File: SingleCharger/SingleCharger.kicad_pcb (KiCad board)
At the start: 2 copper layers, 120 x 130 mm, 59 parts, among them J1 Bus_PCI_Express_x1, Q2 TPHR8504PL,LQ(M1W, U1 ADS1115IDGSR, U10 LM358, U11 MCP4725A0T-E/CH, U2 PICO, U3 TPS54360BDDAR, U4 TPS54360BDDAR, U8 UCC27324DR, U9 LM393

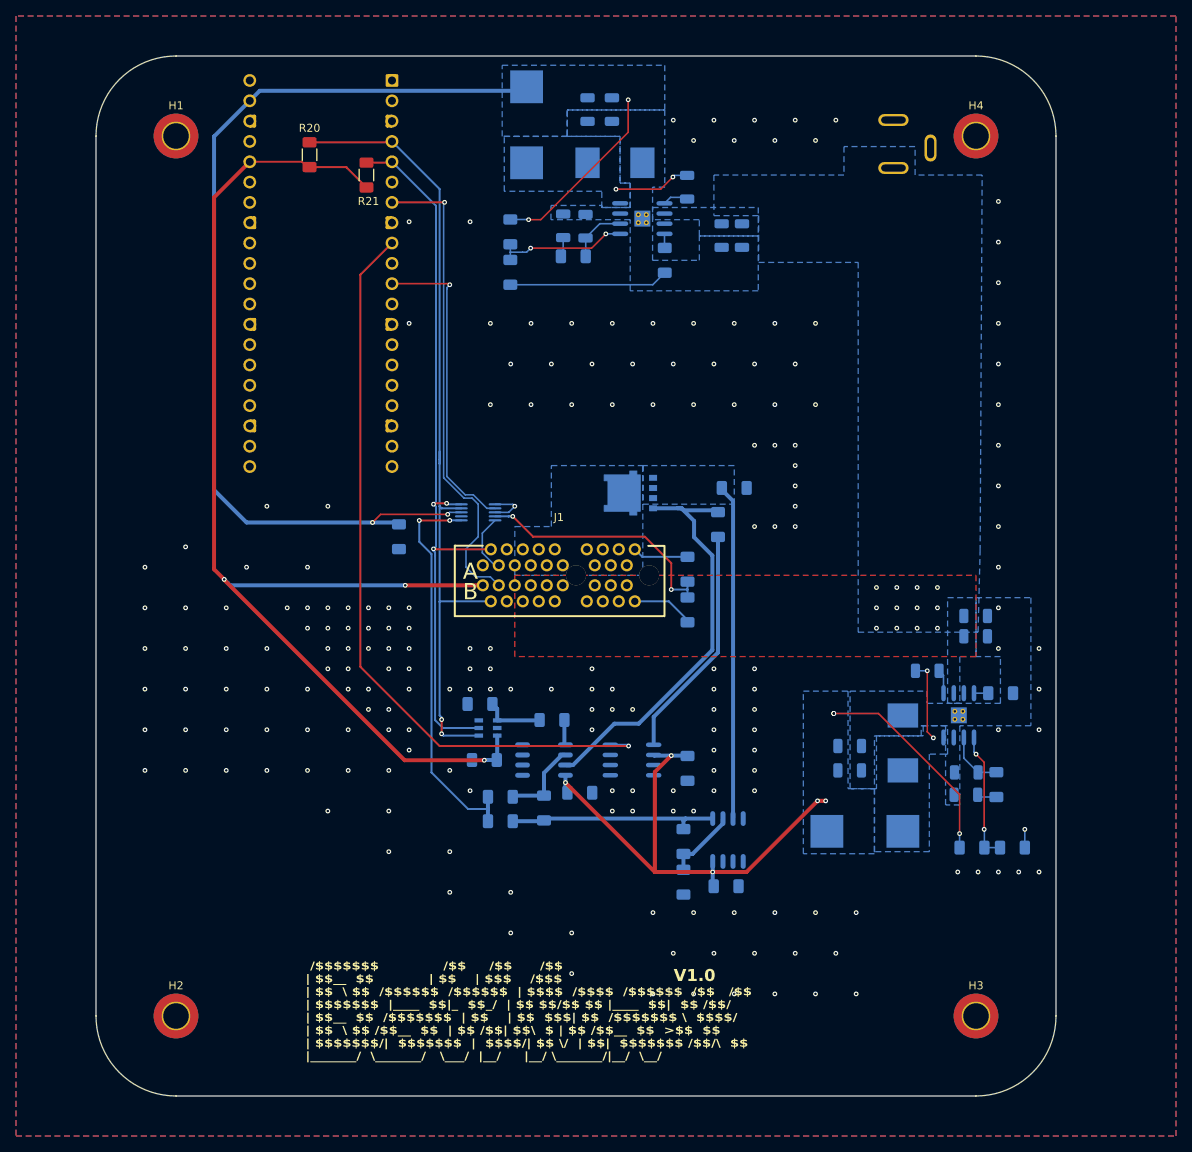
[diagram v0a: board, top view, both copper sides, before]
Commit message: Moved to +48V Feed. 25.2 Controlled by Pico.
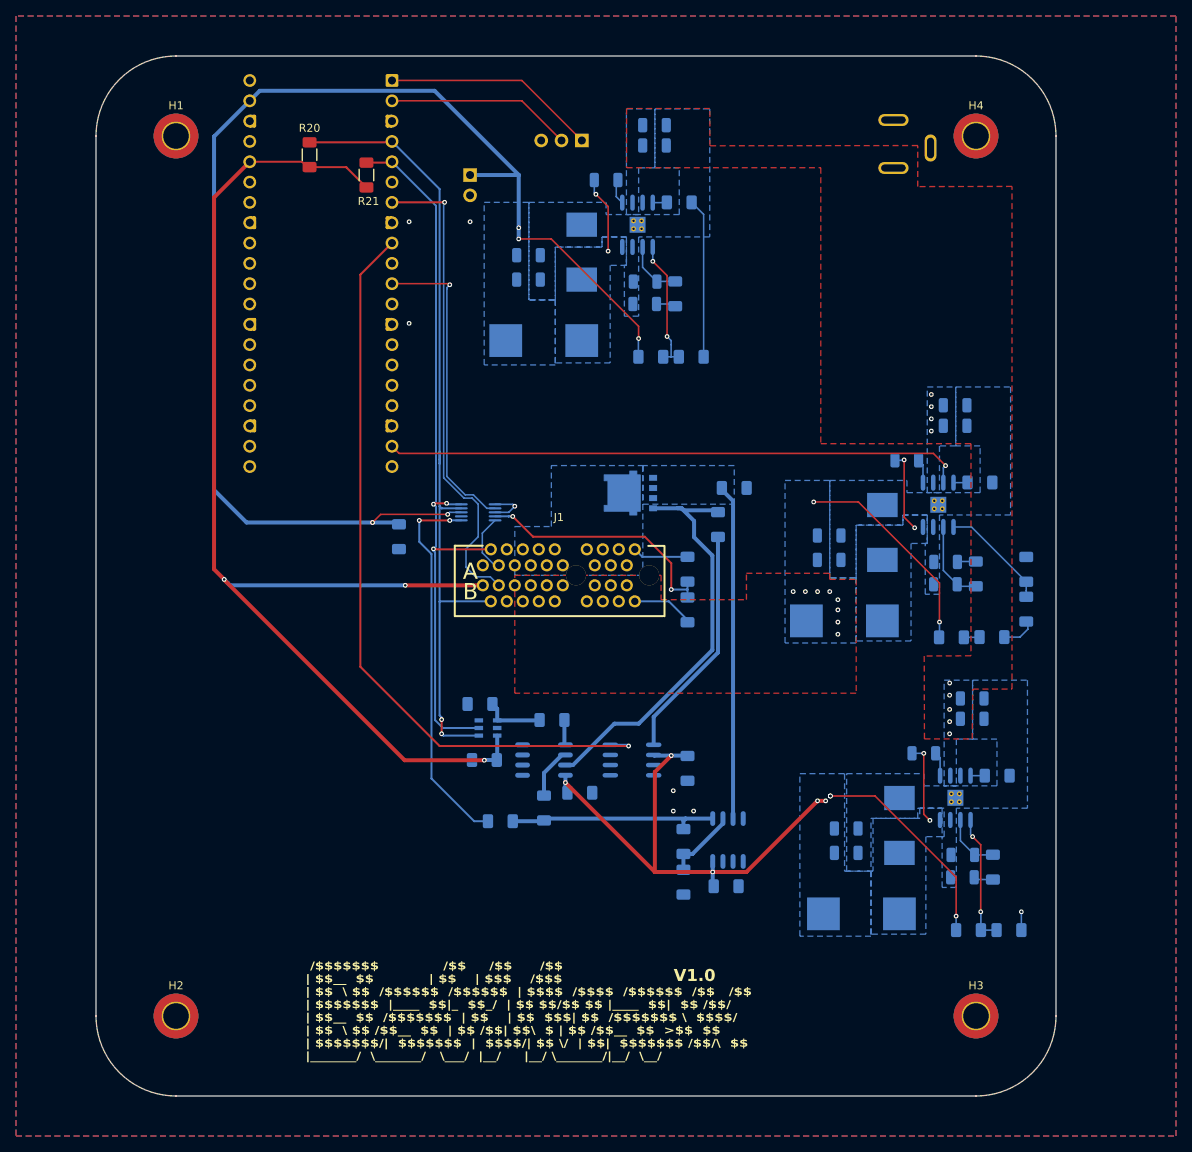
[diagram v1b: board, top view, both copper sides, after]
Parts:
- added C15: 2.2u, Capacitor_SMD:C_1206_3216Metric, B.Cu at (172.4, 71.2)
- added C16: 2.2u, Capacitor_SMD:C_1206_3216Metric, B.Cu at (172.4, 68.7)
- added C20: 0.1u, Capacitor_SMD:C_1206_3216Metric, B.Cu at (166.3, 75.5)
- added C21: 6800p, Capacitor_SMD:C_1206_3216Metric, B.Cu at (171.2, 88.2)
- added C25: 47u, Capacitor_SMD:C_1206_3216Metric, B.Cu at (156.6, 88.0)
- added C26: 39p, Capacitor_SMD:C_1206_3216Metric, B.Cu at (171.2, 91.0)
- added C27: 47u, Capacitor_SMD:C_1206_3216Metric, B.Cu at (156.6, 84.9)
- added D3: B560C-13-F, COMPONENTS:SMC_L7.1-W6.2-LS8.1-RD, B.Cu at (163.3, 84.6)
- added J2: Conn_01x03_Pin, Connector_PinHeader_2.54mm:PinHeader_1x03_P2.54mm_Vertical, B.Cu at (125.7, 35.6)
- added J3: Conn_01x02_Pin, Connector_PinHeader_2.54mm:PinHeader_1x02_P2.54mm_Vertical, B.Cu at (111.8, 39.9)
- added L3: FXL1040-8R2-M, COMPONENTS:IND-SMD_L11.5-W10.0_FXL1040, B.Cu at (158.5, 95.6)
- added R26: 13k, Resistor_SMD:R_1206_3216Metric_Pad1.30x1.75mm_HandSolder, B.Cu at (175.0, 89.7)
- added R27: 300K, Resistor_SMD:R_1206_3216Metric_Pad1.30x1.75mm_HandSolder, B.Cu at (171.9, 97.7)
- added R28: 10k, Resistor_SMD:R_1206_3216Metric_Pad1.30x1.75mm_HandSolder, B.Cu at (181.3, 89.2)
- added R29: 3k, Resistor_SMD:R_1206_3216Metric_Pad1.30x1.75mm_HandSolder, B.Cu at (177.0, 97.6)
- added R30: 2k, Resistor_SMD:R_1206_3216Metric_Pad1.30x1.75mm_HandSolder, B.Cu at (181.3, 94.1)
- added U5: TPS54360BDDAR, COMPONENTS:SOIC-8_L5.0-W4.0-P1.27-LS6.0-BL-EP2.0, B.Cu at (170.3, 81.1)
- R24: value 1k -> 162k
- moved R24 71.7 mm to (175.5, 78.3), turned to 0 degrees
- moved L1 27.1 mm to (121.0, 60.6), turned to 180 degrees
- moved R15 25.0 mm to (139.4, 62.6), turned to 0 degrees
- moved R8 23.5 mm to (134.4, 62.6), turned to 0 degrees
- moved C6 22.5 mm to (119.1, 52.9), turned to 0 degrees
- moved C7 21.0 mm to (119.1, 49.9), turned to 0 degrees
- moved C2 17.6 mm to (134.8, 33.6), turned to 0 degrees
- moved C4 14.1 mm to (133.6, 56.0), turned to 180 degrees
- moved C1 14.0 mm to (134.8, 36.2), turned to 0 degrees
- moved R7 13.6 mm to (137.4, 54.7), turned to -90 degrees
- moved D1 11.9 mm to (125.7, 49.5), turned to 90 degrees
- moved R17 10.3 mm to (177.1, 126.4)
- moved R18 10.3 mm to (174.1, 134.3)
- moved R19 10.3 mm to (179.1, 134.3)
- moved C10 10.3 mm to (168.5, 112.2)
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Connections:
- C1 pad 1: +24V -> +48V
- C2 pad 1: +24V -> +48V
- C8 pad 1: +24V -> +48V
- C9 pad 1: +24V -> +48V
- DC1 pad 1: +24V -> +48V
- R24 pad 1: Net-(U9B--) -> Net-(U5-RT/CLK)
- R24 pad 2: /BatteryCC/RSns Charge -> GND
- U2 pad 1: unconnected-(U2-GP0-Pad1) -> Net-(J2-Pin_1)
- U2 pad 19: unconnected-(U2-GP14-Pad19) -> /Power Delivery/EN_BAT_V
- U2 pad 2: unconnected-(U2-GP1-Pad2) -> Net-(J2-Pin_2)
- U3 pad 2: +24V -> +48V
- U4 pad 2: +24V -> +48V
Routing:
- net /Power Delivery/EN_BAT_V: track 0.00 -> 72.4 mm, vias 0 -> 1
- net Net-(J2-Pin_1): track 0.00 -> 26.8 mm
- net +24V: track 7.84 -> 34.4 mm, vias 12 -> 10
- net Net-(J2-Pin_2): track 0.00 -> 23.2 mm
- net +5V: track 145.7 -> 163.6 mm, vias 4 -> 5
- net /Power Delivery/FB24: track 0.00 -> 13.8 mm
- net Net-(U5-COMP): track 0.00 -> 10.3 mm
- net Net-(D3-K): track 0.00 -> 10.2 mm, vias 0 -> 2
- net Net-(R29-Pad2): track 0.00 -> 4.39 mm
- net Net-(U9B--): track 10.4 -> 6.45 mm
- net Net-(U5-BOOT): track 0.00 -> 3.02 mm
- net Net-(C21-Pad1): track 0.00 -> 2.33 mm
- net /BatteryCC/RSns Charge: track 49.4 -> 47.4 mm
- net Net-(R27-Pad2): track 0.00 -> 1.97 mm
- net Net-(U5-RT/CLK): track 0.00 -> 1.76 mm
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- added copper zone on B.Cu, net +48V
- added copper zone on F.Cu, net +48V
- added copper zone on B.Cu, net Net-(D3-K)

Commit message: Updated Production Files.
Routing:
- net GND: vias 8 -> 162

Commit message: Updated Version, and Production Files.
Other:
- board text added: "V1.1"
- board text removed: "V1.0"
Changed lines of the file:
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@@
 		)
 		(embedded_fonts no)
-		(model "/COMPONENTS.3dshapes/SMC_L7.1-W6.2-LS8.1-RD.wrl"
+		(model "${COMPONENTS_3D_MODELS}/SMC_L7.1-W6.2-LS8.1-RD.step"
 			(offset
 				(xyz 0 -0 -0)
@@
 		)
 		(property "Datasheet" ""
-			(at 0 0 -90)
+			(at 0 0 270)
 			(unlocked yes)
 			(layer "B.Fab")
@@
 		)
 		(property "Description" "Generic connector, single row, 01x03, script generated"
-			(at 0 0 -90)
+			(at 0 0 270)
 			(unlocked yes)
 			(layer "B.Fab")
@@
 		)
 		(embedded_fonts no)
-		(model "/COMPONENTS.3dshapes/SOIC-8_L4.9-W3.9-H1.7-LS6.0-P1.27.wrl"
+		(model "${COMPONENTS_3D_MODELS}/SOIC-8_L4.9-W3.9-H1.7-LS6.0-P1.27.step"
 			(offset
-				(xyz -942.57 832.23 -0)
+				(xyz 0 0 -0)
 			)
 			(scale
@@
 			)
 			(rotate
-				(xyz 0 0 0)
+				(xyz -0 -0 -0)
 			)
 		)
@@
 		)
 		(embedded_fonts no)
-		(model "/COMPONENTS.3dshapes/IND-SMD_L11.5-W10.0-H3.8_FXL1040.wrl"
+		(model "${COMPONENTS_3D_MODELS}/IND-SMD_L11.5-W10.0-H3.8_FXL1040.step"
 			(offset
 				(xyz 0 -0 -0)
@@
 		)
 	)
-	(gr_text "V1.0"
+	(gr_text "V1.1"
 		(at 139.827 139.9286 0)
 		(layer "F.SilkS" knockout)
 		(effects
 			(font
-				(face "Segoe UI Historic")
+				(face "Futura")
 				(size 1.5 1.5)
 				(thickness 0.3)
@@
 			)
 		)
-		(render_cache "V1.0" 0
+		(render_cache "V1.1" 0
 			(polygon
 				(pts
-					(xy 139.108468 139.073919) (xy 138.562127 140.5511) (xy 138.368595 140.5511) (xy 137.83352 139.073919)
-					(xy 138.031448 139.073919) (xy 138.438937 140.242529) (xy 138.455702 140.301387) (xy 138.468429 140.370848)
-					(xy 138.467422 140.370848) (xy 138.479252 140.310564) (xy 138.501036 140.240423) (xy 138.916676 139.073919)
+					(xy 137.778657 138.965475) (xy 138.160867 139.930753) (xy 138.545091 138.965475) (xy 138.992422 138.965475)
+					(xy 138.324632 140.5511) (xy 137.99701 140.5511) (xy 137.331327 138.965475)
 				)
 			)
 			(polygon
 				(pts
-					(xy 139.868399 140.5511) (xy 139.694467 140.5511) (xy 139.694467 139.284853) (xy 139.642169 139.324787)
-					(xy 139.557905 139.374612) (xy 139.459261 139.420866) (xy 139.354298 139.455762) (xy 139.354298 139.279632)
-					(xy 139.473458 139.23805) (xy 139.595091 139.180348) (xy 139.708023 139.113578) (xy 139.800805 139.04461)
-					(xy 139.868399 139.04461)
+					(xy 139.548563 139.314254) (xy 139.317021 139.314254) (xy 139.317021 138.962544) (xy 139.958891 138.962544)
+					(xy 139.958891 140.5511) (xy 139.548563 140.5511)
 				)
 			)
 			(polygon
 				(pts
-					(xy 140.483433 140.574547) (xy 140.438631 140.565964) (xy 140.400909 140.5402) (xy 140.375259 140.502329)
-					(xy 140.366746 140.45786) (xy 140.375248 140.413233) (xy 140.400909 140.37497) (xy 140.438674 140.348776)
-					(xy 140.483433 140.340074) (xy 140.529137 140.348807) (xy 140.567422 140.37497) (xy 140.593513 140.413275)
-					(xy 140.602135 140.45786) (xy 140.593503 140.502287) (xy 140.567422 140.5402) (xy 140.52918 140.565933)
+					(xy 140.438096 140.351706) (xy 140.442866 140.302459) (xy 140.457055 140.256085) (xy 140.479778 140.213596)
+					(xy 140.509628 140.177225) (xy 140.546067 140.147292) (xy 140.588488 140.12456) (xy 140.634887 140.110375)
+					(xy 140.684292 140.105601) (xy 140.733698 140.110375) (xy 140.780097 140.12456) (xy 140.822578 140.147302)
+					(xy 140.858956 140.177225) (xy 140.888859 140.213606) (xy 140.91153 140.256085) (xy 140.925719 140.302459)
+					(xy 140.930489 140.351706) (xy 140.925715 140.401111) (xy 140.91153 140.44751) (xy 140.888863 140.490005)
+					(xy 140.858956 140.526462) (xy 140.822585 140.556311) (xy 140.780097 140.579035) (xy 140.733698 140.59322)
+					(xy 140.684292 140.597994) (xy 140.634887 140.59322) (xy 140.588488 140.579035) (xy 140.54606 140.556321)
+					(xy 140.509628 140.526462) (xy 140.479774 140.490015) (xy 140.457055 140.44751) (xy 140.44287 140.401111)
 				)
 			)
 			(polygon
 				(pts
-					(xy 141.385257 139.058901) (xy 141.465097 139.082962) (xy 141.534308 139.121944) (xy 141.594692 139.176671)
-					(xy 141.64707 139.24942) (xy 141.691208 139.343727) (xy 141.725854 139.464164) (xy 141.748853 139.61615)
-					(xy 141.757281 139.805823) (xy 141.748411 139.984941) (xy 141.723851 140.133261) (xy 141.697135 140.226831)
-					(xy 141.664714 140.306589) (xy 141.62713 140.374237) (xy 141.580784 140.435497) (xy 141.529006 140.484867)
-					(xy 141.471426 140.523531) (xy 141.408058 140.551523) (xy 141.338507 140.568649) (xy 141.261499 140.574547)
-					(xy 141.188548 140.568882) (xy 141.122739 140.552436) (xy 141.062838 140.525546) (xy 141.008479 140.488557)
-					(xy 140.959559 140.4414) (xy 140.915743 140.382938) (xy 140.864563 140.281997) (xy 140.825159 140.153228)
-					(xy 140.802547 140.011967) (xy 140.794384 139.841727) (xy 140.794734 139.834125) (xy 140.972438 139.834125)
-					(xy 140.982087 140.026468) (xy 141.00752 140.168444) (xy 141.044391 140.270701) (xy 141.089847 140.342236)
-					(xy 141.142886 140.389988) (xy 141.204575 140.418235) (xy 141.277894 140.428001) (xy 141.349612 140.418234)
-					(xy 141.410185 140.389894) (xy 141.462525 140.34174) (xy 141.5076 140.26921) (xy 141.544299 140.165045)
-					(xy 141.569678 140.019904) (xy 141.57932 139.822767) (xy 141.569677 139.617043) (xy 141.544356 139.466219)
-					(xy 141.507889 139.358605) (xy 141.463373 139.284254) (xy 141.412096 139.235338) (xy 141.353252 139.206798)
-					(xy 141.28403 139.197017) (xy 141.210262 139.207189) (xy 141.147822 139.236759) (xy 141.093716 139.287149)
-					(xy 141.046993 139.363278) (xy 141.008873 139.472901) (xy 140.982475 139.62595) (xy 140.972438 139.834125)
-					(xy 140.794734 139.834125) (xy 140.802992 139.654744) (xy 140.826716 139.5011) (xy 140.852948 139.404021)
-					(xy 140.884909 139.321955) (xy 140.921971 139.252979) (xy 140.968233 139.190425) (xy 141.020187 139.140392)
-					(xy 141.078225 139.101579) (xy 141.142279 139.073601) (xy 141.213146 139.056412) (xy 141.292182 139.050471)
+					(xy 141.452192 139.314254) (xy 141.22065 139.314254) (xy 141.22065 138.962544) (xy 141.86252 138.962544)
+					(xy 141.86252 140.5511) (xy 141.452192 140.5511)
 				)
 			)

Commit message: Added SCL/SDA Pins.
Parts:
- added J4: Conn_01x02_Pin, Connector_PinHeader_2.54mm:PinHeader_1x02_P2.54mm_Vertical, F.Cu at (73.4, 61.2)
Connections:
- U2 pad 26: unconnected-(U2-GP20-Pad26) -> /SDA0
- U2 pad 27: unconnected-(U2-GP21-Pad27) -> /SCL0
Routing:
- net /SDA0: track 0.00 -> 10.9 mm, vias 0 -> 1
- net /SCL0: track 0.00 -> 10.9 mm, vias 0 -> 1
- net +5V: track 163.6 -> 167.0 mm
- net GND: vias 162 -> 188
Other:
- board text added: "2k"
- board text added: "300K"
- board text added: "3k"
- board text added: "5v"
- board text added: "gnd"
- board text added: "rx"
- board text added: "scl"
- board text added: "sda"
- board text added: "tx"
